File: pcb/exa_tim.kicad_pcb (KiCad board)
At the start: 4 copper layers, 42 x 42 mm, 51 parts, among them J1 20021112-00010T4LF, J2 FH12-24S-0.5SH(55), Q1 SI2333DS-T1-E3, Q2 DMN3067LW-7, SW1 TL3305CF260QG, SW2 TL3305CF260QG, SW3 TL3305CF260QG, SW4 TL3305CF260QG, U1 STM32L071KZUx, U2 CAM-M8C-0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

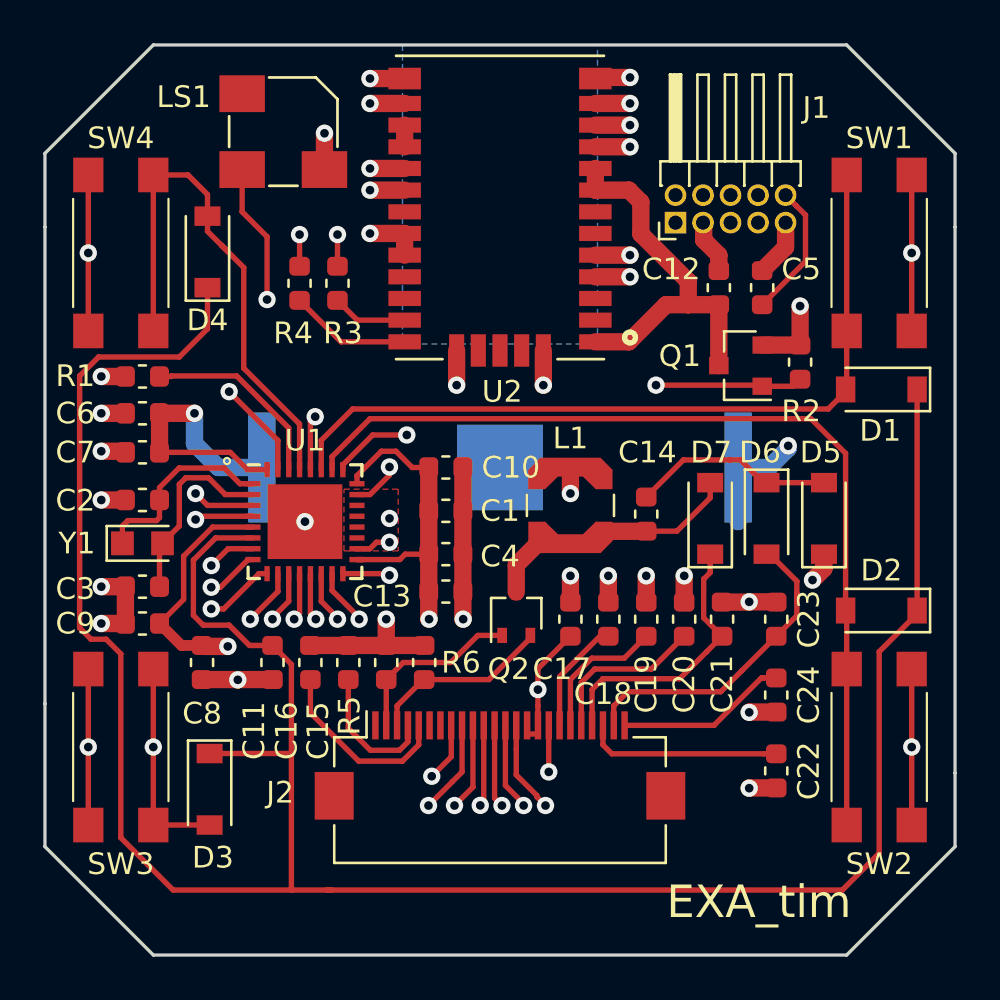
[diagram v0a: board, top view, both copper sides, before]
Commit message: Second pass to reloacte many components up for connector placement
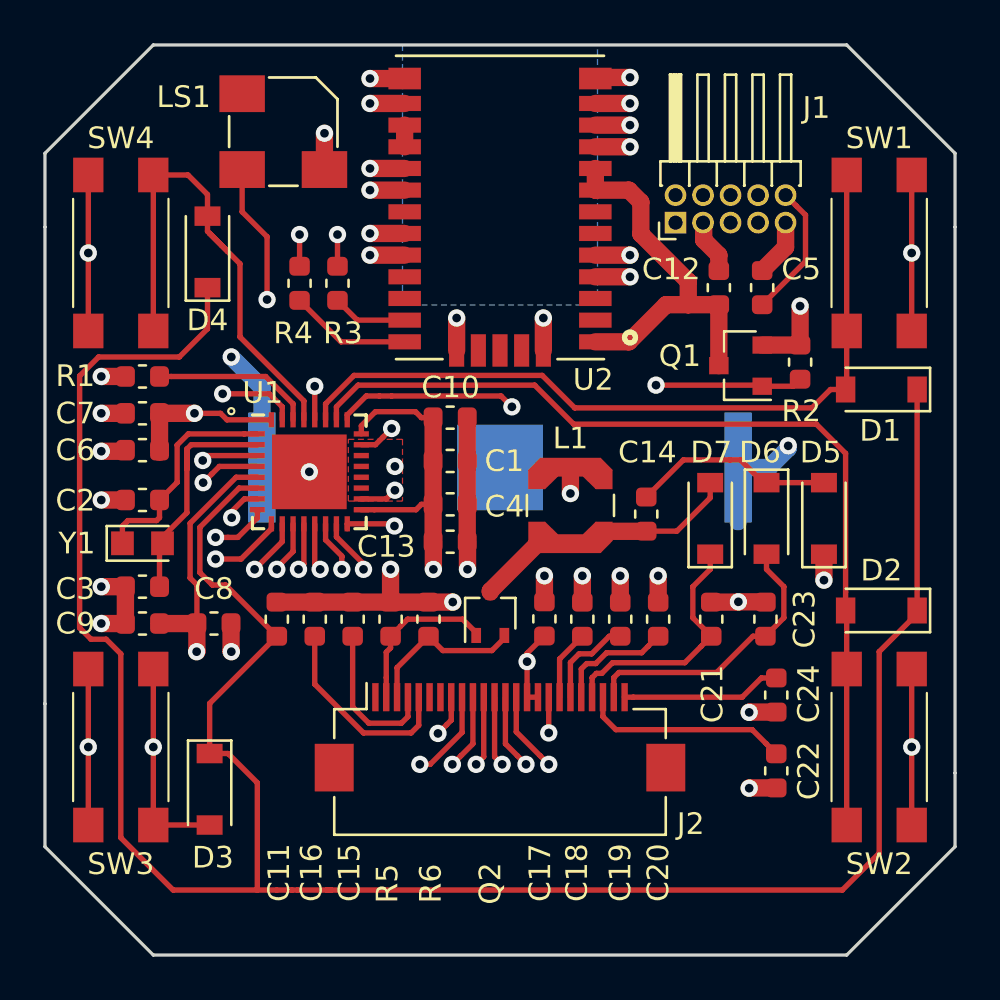
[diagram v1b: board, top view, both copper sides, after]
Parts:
- moved C1 2.31 mm to (118.7, 89.2)
- moved C10 2.31 mm to (118.7, 87.2)
- moved C13 2.31 mm to (118.7, 92.9)
- moved C4 2.31 mm to (118.7, 91.2)
- moved U1 2.31 mm to (112.2, 89.7)
- moved C11 2.01 mm to (110.7, 96.5), turned to 90 degrees
- moved C15 2.01 mm to (114.2, 96.5)
- moved C16 2.01 mm to (112.5, 96.5)
- moved R5 2.01 mm to (116.0, 96.5)
- moved R6 2.01 mm to (117.7, 96.5)
- moved C8 1.88 mm to (107.8, 96.7), turned to 180 degrees
- moved C7 1.80 mm to (104.5, 87.0)
- moved C6 1.70 mm to (104.5, 88.7)
- moved J2 1.30 mm to (121.0, 102.0)
- moved C17 1.20 mm to (123.0, 96.5)
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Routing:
- net GND: track 85.5 -> 79.3 mm, vias 38 -> 40
- net /BTN3: track 30.7 -> 35.6 mm
- net /NRST: track 49.6 -> 44.9 mm
- net /SWDIO: track 24.3 -> 21.7 mm
- net 3V: track 86.6 -> 84.0 mm, vias 11 -> 12
- net Net-(C18-Pad1): track 5.58 -> 3.25 mm
- net /TX: track 24.3 -> 21.9 mm
- net /SWCLK: track 26.9 -> 24.6 mm
- net Net-(C3-Pad1): track 9.62 -> 11.8 mm
- net Net-(C20-Pad1): track 7.61 -> 5.48 mm
- net Net-(C19-Pad1): track 6.50 -> 4.40 mm
- net /RX: track 29.9 -> 27.8 mm
- net /ALARM: track 23.5 -> 21.6 mm
- net /PREVGL: track 15.0 -> 13.3 mm
- net /GNSS_EN: track 34.1 -> 32.6 mm
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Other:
- board text added: "DC 180917"
- board text removed: "DC 180916"

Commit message: Redesigned LSE layout and re-routed some traces
Also switched BTN3 and BTN4 pins for easier routing.
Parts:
- added R7: 0, Resistor_SMD:R_0603_1608Metric, B.Cu at (104.4, 89.9)
- moved C2 3.17 mm to (103.5, 94.0), turned to 270 degrees
- moved Y1 1.50 mm to (104.4, 91.5)
- moved C3 1.30 mm to (105.3, 94.0), turned to 270 degrees
- turned D4 to 270 degrees
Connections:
- U1 pad 28: /BTN3 -> /BTN4
- U1 pad 29: /BTN4 -> /BTN3
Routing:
- net 3V: track 84.0 -> 67.1 mm, vias 12 -> 16
- net GND: track 79.3 -> 94.0 mm, vias 40 -> 38
- net /WKUP1: track 114.9 -> 126.6 mm
- net /NRST: track 44.9 -> 56.4 mm
- net /RX: track 27.8 -> 21.9 mm
- net /BTN3: track 35.6 -> 39.9 mm, vias 2 -> 0
- net Net-(C3-Pad1): track 11.8 -> 8.23 mm
- net /BTN4: track 23.5 -> 20.0 mm
- net /TX: track 21.9 -> 19.5 mm
- net /ALARM: track 21.6 -> 19.4 mm
- net /GNSS_EN: track 32.6 -> 31.3 mm
- added copper zone on B.Cu, net GNDD
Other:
- board text added: "DC 180918"
- board text removed: "DC 180917"

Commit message: Switched LSE crystall for achieving LOW drive capability
It seems my oscilloscope is interfering wit LSE
operation when measuring and having the LOW drive
capability on.

But the LSE seeem to work fine, since the RTC and LPTIM
seem to work fine under it.
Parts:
- Y1: value 9HT11-32.768KDZB-T -> ST2012SB32768B0HPWBB
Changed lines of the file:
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@@
       (effects (font (size 1 1) (thickness 0.15)))
     )
-    (fp_text value 9HT11-32.768KDZB-T (at 0 1.8) (layer F.Fab)
+    (fp_text value ST2012SB32768B0HPWBB (at 0 1.8) (layer F.Fab)
       (effects (font (size 1 1) (thickness 0.15)))
     )

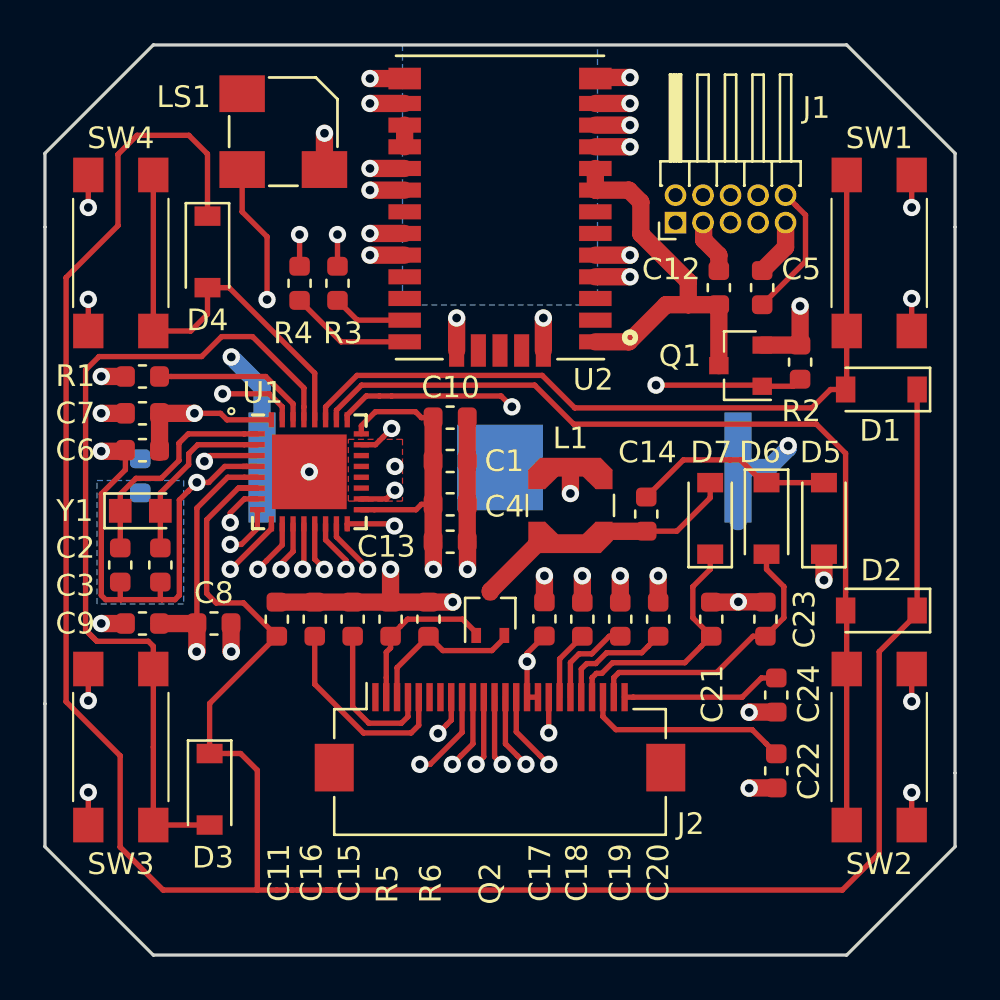
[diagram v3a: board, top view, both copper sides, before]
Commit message: Add third MOSFET to shutdown E-Paper driver
This will cut off the e-paper from any voltage source
and should result in an even lower power usage.
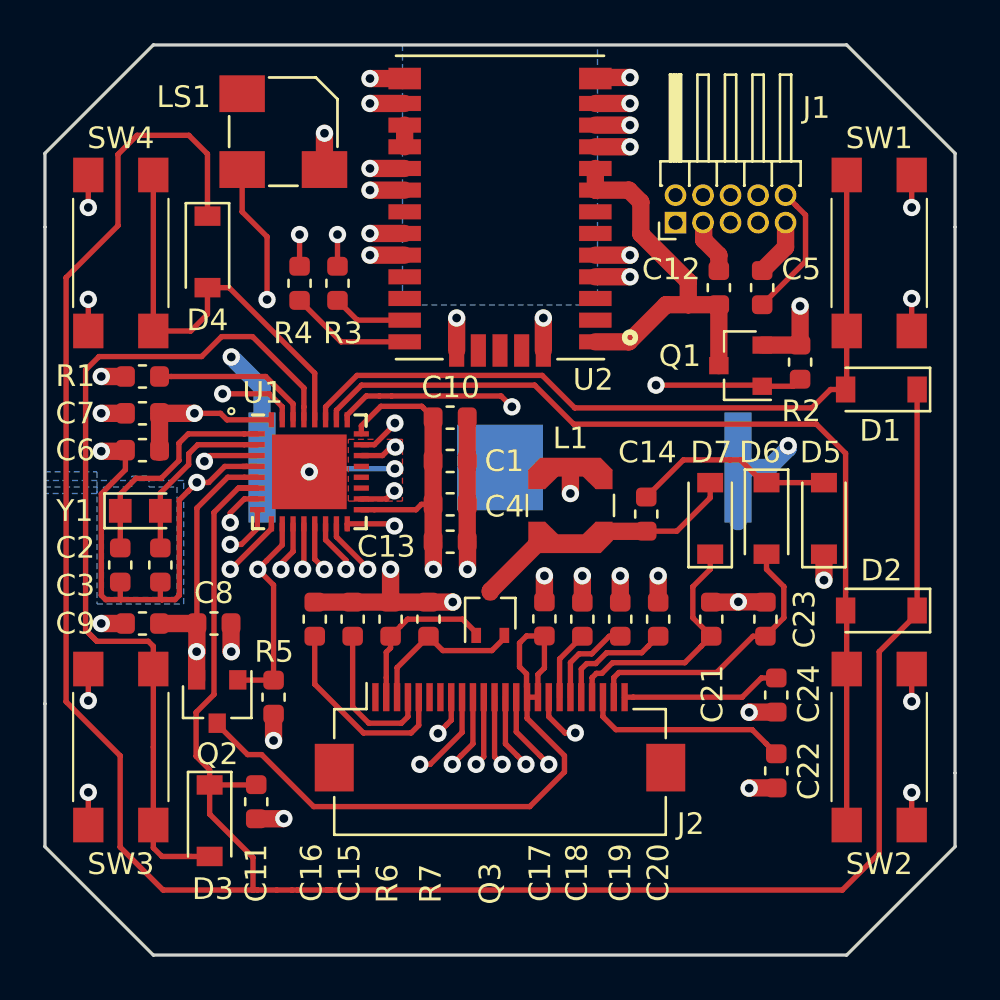
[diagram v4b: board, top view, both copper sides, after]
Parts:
- removed the R7 at (104.4, 89.9)
- added Q2: SI2333DS-T1-E3, Package_TO_SOT_SMD:SOT-23, F.Cu at (108.0, 100.3)
- added R5: 1M, Resistor_SMD:R_0603_1608Metric, F.Cu at (110.5, 100.1)
- moved C11 8.48 mm to (109.8, 104.9), turned to 270 degrees
- moved D3 1.45 mm to (107.6, 105.8)
- renumbered Q2 to Q3, R5 to R6, R6 to R7
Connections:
- C17 pad 1: 3V -> /VDD_DISP
- J2 pad 15: 3V -> /VDD_DISP
- J2 pad 16: 3V -> /VDD_DISP
- U1 pad 10: /GNSS_EN -> /DISP_EN
- U1 pad 22: GND -> /GNSS_EN
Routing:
- net /VDD_DISP: track 0.00 -> 29.9 mm
- net /DISP_EN: track 0.00 -> 9.68 mm, vias 0 -> 1
- net /GNSS_EN: track 31.3 -> 21.8 mm
- net GND: track 94.0 -> 98.3 mm, vias 38 -> 39
- net /WKUP1: track 126.6 -> 124.9 mm
- net /BTN3: track 39.9 -> 41.1 mm
- net 3V: track 67.1 -> 66.2 mm
- removed copper zone on B.Cu, net GNDD
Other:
- board text added: "DC 180920"
- board text removed: "DC 180918"
